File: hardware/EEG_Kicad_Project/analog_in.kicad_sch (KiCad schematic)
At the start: 1 part, among them U3 ADS1299

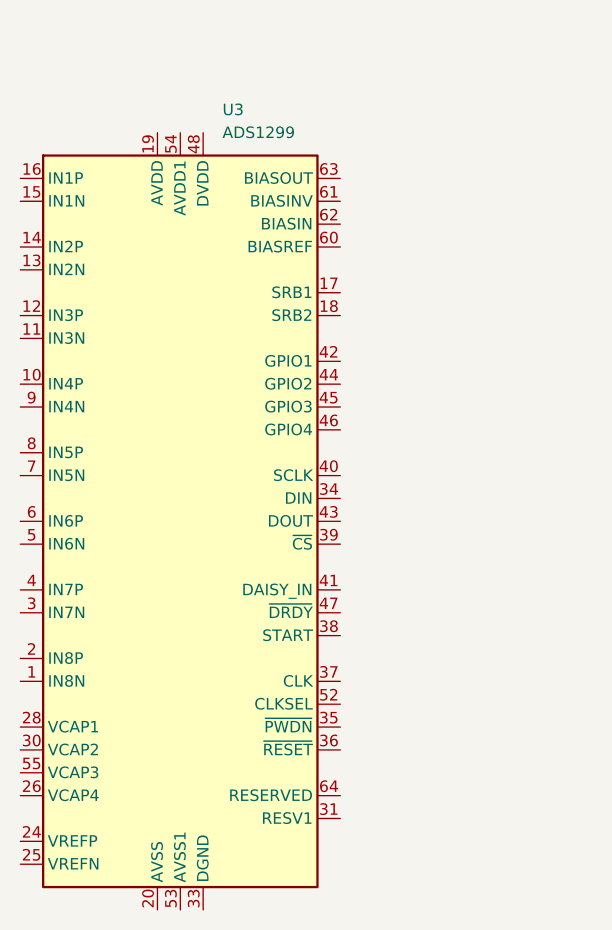
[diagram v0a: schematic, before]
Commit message: Readme change, add -5V, some organizational changes
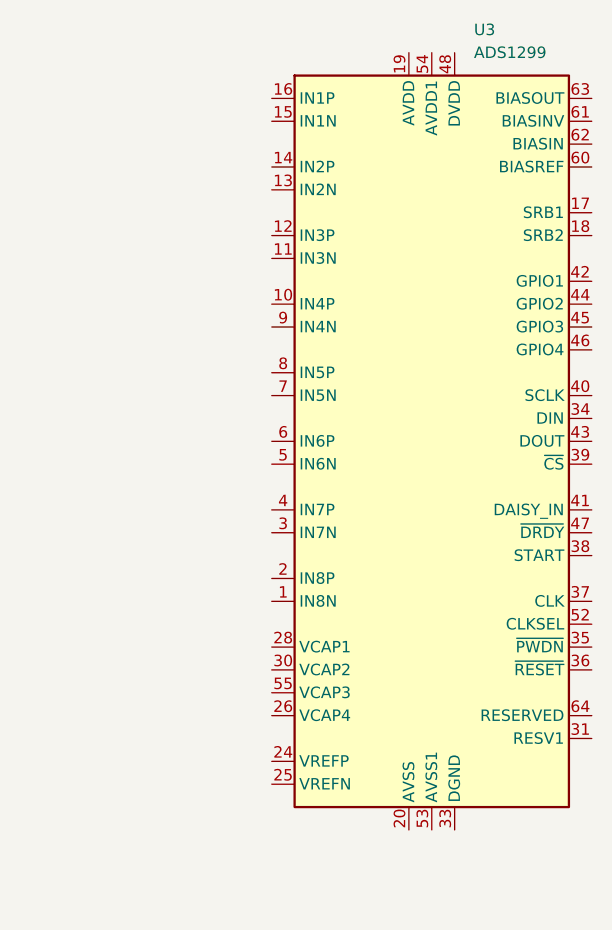
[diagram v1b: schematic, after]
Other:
- moved on the sheet: U3
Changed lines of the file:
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@@
 	(symbol
 		(lib_id "Analog_ADC:ADS1299")
-		(at 189.23 114.3 0)
+		(at 217.17 105.41 0)
 		(unit 1)
 		(exclude_from_sim no)
@@
 		(fields_autoplaced yes)
 		(property "Reference" "U3"
-			(at 193.9133 68.58 0)
+			(at 221.8533 59.69 0)
 			(effects
 				(font
@@
 		)
 		(property "Value" "ADS1299"
-			(at 193.9133 71.12 0)
+			(at 221.8533 62.23 0)
 			(effects
 				(font
@@
 		)
 		(property "Footprint" "Package_QFP:TQFP-64_10x10mm_P0.5mm"
-			(at 189.23 167.64 0)
+			(at 217.17 158.75 0)
 			(effects
 				(font
@@
 		)
 		(property "Datasheet" "https://www.ti.com/lit/ds/symlink/ads1299.pdf"
-			(at 189.23 170.18 0)
+			(at 217.17 161.29 0)
 			(effects
 				(font
@@
 		)
 		(property "Description" "Low-Noise, 8-channel, 24-bit ADC for EEG and Biopotential Measurements, TQFP-64"
-			(at 189.23 116.84 0)
+			(at 217.17 107.95 0)
 			(effects
 				(font
